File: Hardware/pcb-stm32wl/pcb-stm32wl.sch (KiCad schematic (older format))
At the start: 0 parts

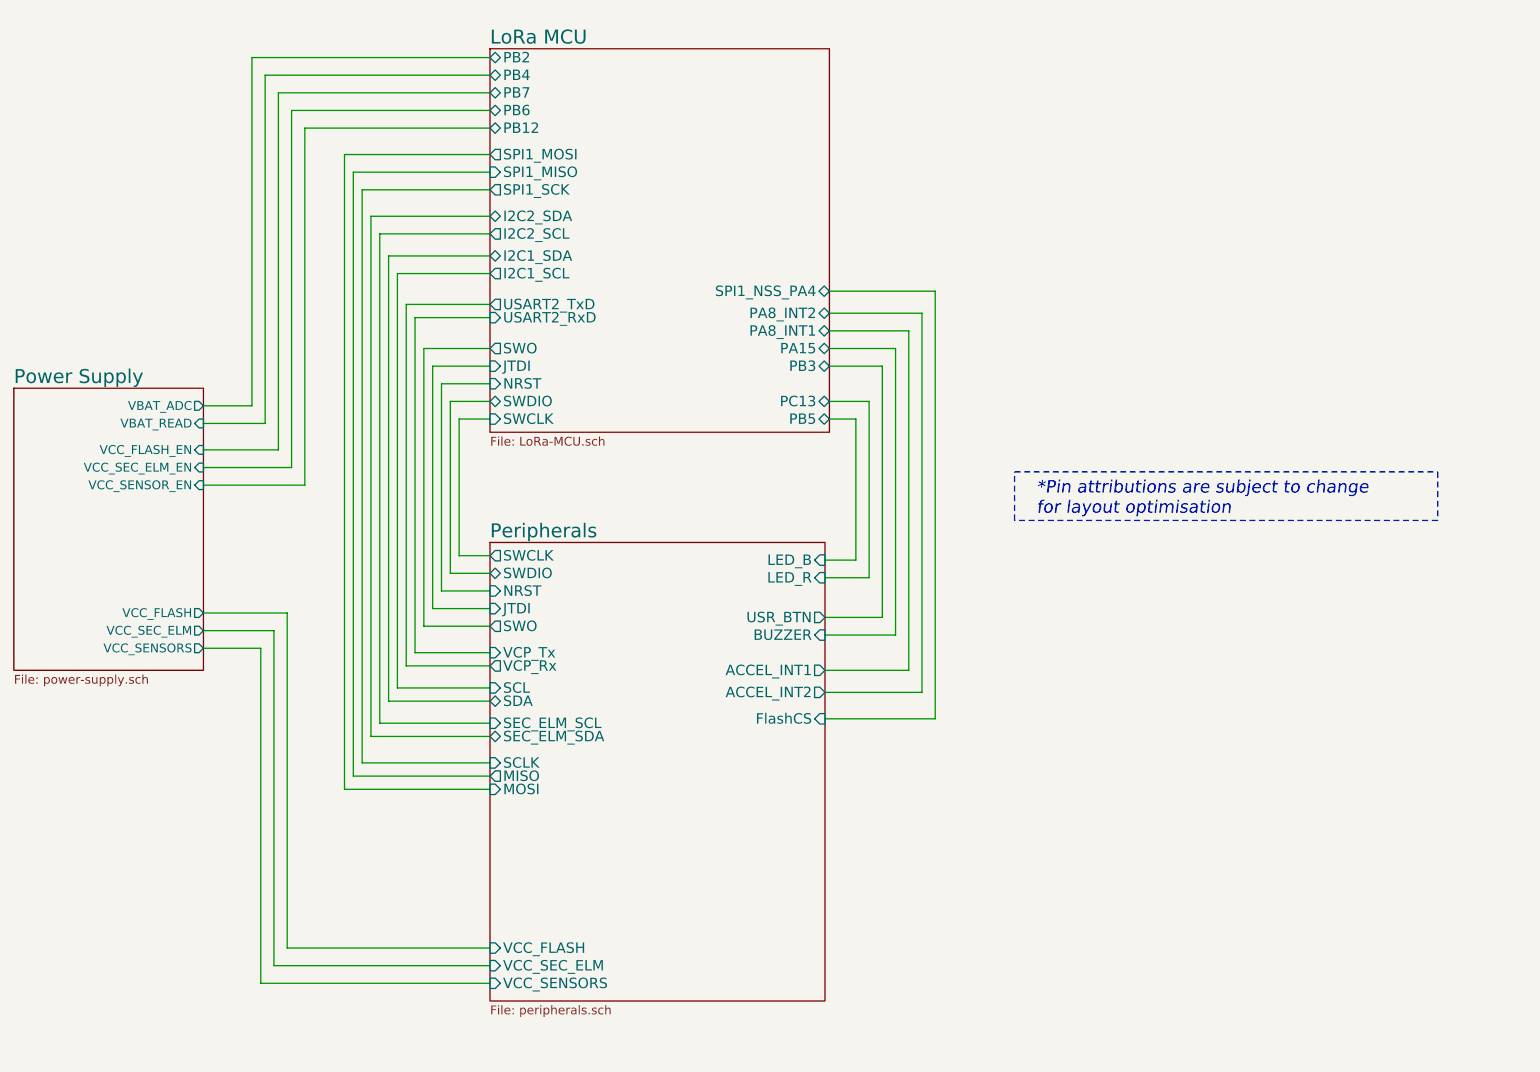
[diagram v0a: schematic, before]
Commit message: pcb,sch: Add V0.2 HW design with external battery holder
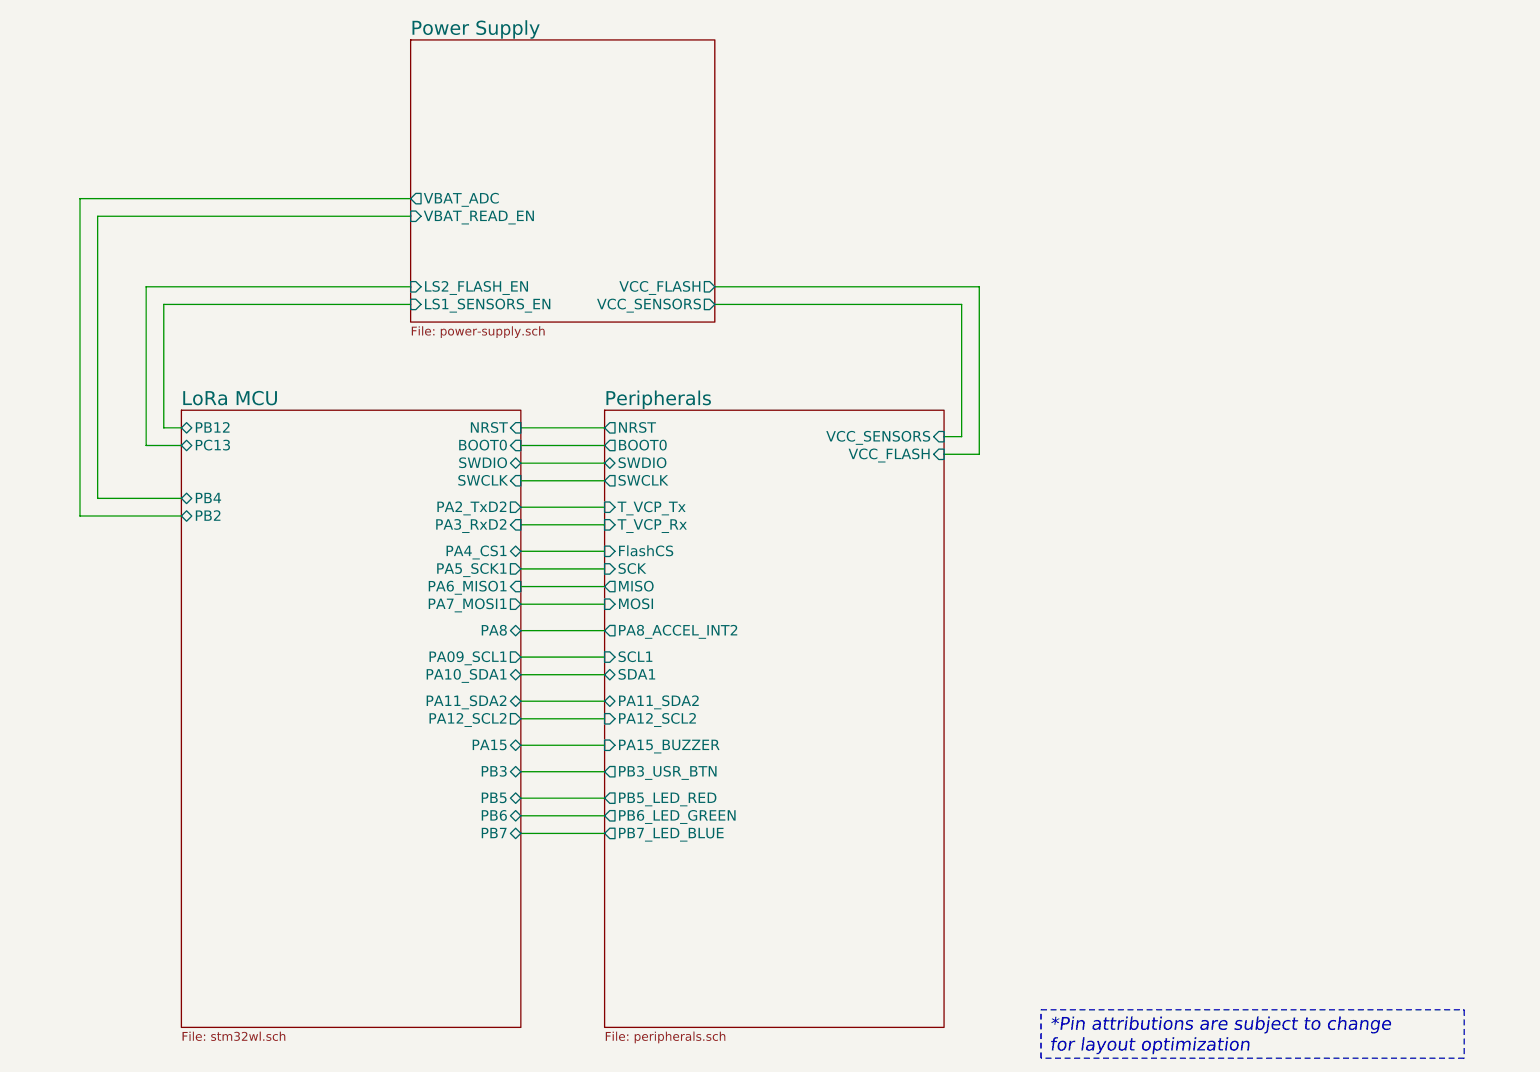
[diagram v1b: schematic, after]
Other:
- note added: "*Pin attributions are subject to change \nfor layout optimization"
- note removed: "*Pin attributions are subject to change \nfor layout optimisation"
